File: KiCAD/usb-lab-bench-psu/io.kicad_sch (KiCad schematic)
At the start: 14 parts, among them J9 X077-6428TSWCG01-H13, Q6 2N7002K, Q7 BSS84

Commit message: updated GND and supply nets, switched buck-boost-converter
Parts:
- renumbered C41 to C30, C42 to C31, C43 to C32, C47 to C33, C48 to C34, Q6 to Q3, Q7 to Q4, R54 to R34, R53 to R35, R49 to R36, R50 to R37, R51 to R38, R52 to R39
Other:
- removed sheet 3.3V Buck Converter1
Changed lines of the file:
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@@
 		(dnp no)
 		(fields_autoplaced yes)
-		(property "Reference" "R53"
+		(property "Reference" "R35"
 			(at 35.56 34.2899 0)
 			(effects
@@
 			(project ""
 				(path "/63928bc9-e618-488a-a687-c6d5597f31d9/a5b1ba07-0ccc-4e60-84be-65366c488a00"
-					(reference "R53")
+					(reference "R35")
 					(unit 1)
 				)
@@
 		(on_board yes)
 		(dnp no)
-		(property "Reference" "R51"
+		(property "Reference" "R38"
 			(at 201.295 64.77 90)
 			(effects
@@
 			(project "usb-lab-bench-psu"
 				(path "/63928bc9-e618-488a-a687-c6d5597f31d9/a5b1ba07-0ccc-4e60-84be-65366c488a00"
-					(reference "R51")
+					(reference "R38")
 					(unit 1)
 				)
@@
 		(dnp no)
 		(fields_autoplaced yes)
-		(property "Reference" "R50"
+		(property "Reference" "R37"
 			(at 101.6 33.02 90)
 			(effects
@@
 			(project "usb-lab-bench-psu"
 				(path "/63928bc9-e618-488a-a687-c6d5597f31d9/a5b1ba07-0ccc-4e60-84be-65366c488a00"
-					(reference "R50")
+					(reference "R37")
 					(unit 1)
 				)
@@
 		(dnp no)
 		(fields_autoplaced yes)
-		(property "Reference" "C48"
+		(property "Reference" "C34"
 			(at 166.37 78.7399 0)
 			(effects
@@
 			(project "usb-lab-bench-psu"
 				(path "/63928bc9-e618-488a-a687-c6d5597f31d9/a5b1ba07-0ccc-4e60-84be-65366c488a00"
-					(reference "C48")
+					(reference "C34")
 					(unit 1)
 				)
@@
 		(dnp no)
 		(fields_autoplaced yes)
-		(property "Reference" "Q6"
+		(property "Reference" "Q3"
 			(at 114.3 46.9899 0)
 			(effects
@@
 			(project "usb-lab-bench-psu"
 				(path "/63928bc9-e618-488a-a687-c6d5597f31d9/a5b1ba07-0ccc-4e60-84be-65366c488a00"
-					(reference "Q6")
+					(reference "Q3")
 					(unit 1)
 				)
@@
 		(dnp no)
 		(fields_autoplaced yes)
-		(property "Reference" "C41"
+		(property "Reference" "C30"
 			(at 133.35 58.4199 0)
 			(effects
@@
 			(project "usb-lab-bench-psu"
 				(path "/63928bc9-e618-488a-a687-c6d5597f31d9/a5b1ba07-0ccc-4e60-84be-65366c488a00"
-					(reference "C41")
+					(reference "C30")
 					(unit 1)
 				)
@@
 		(dnp no)
 		(fields_autoplaced yes)
-		(property "Reference" "Q7"
+		(property "Reference" "Q4"
 			(at 133.35 38.0999 0)
 			(effects
@@
 			(project "usb-lab-bench-psu"
 				(path "/63928bc9-e618-488a-a687-c6d5597f31d9/a5b1ba07-0ccc-4e60-84be-65366c488a00"
-					(reference "Q7")
+					(reference "Q4")
 					(unit 1)
 				)
@@
 		(dnp no)
 		(fields_autoplaced yes)
-		(property "Reference" "C47"
+		(property "Reference" "C33"
 			(at 156.21 58.4199 0)
 			(effects
@@
 			(project "usb-lab-bench-psu"
 				(path "/63928bc9-e618-488a-a687-c6d5597f31d9/a5b1ba07-0ccc-4e60-84be-65366c488a00"
-					(reference "C47")
+					(reference "C33")
 					(unit 1)
 				)
@@
 		(on_board yes)
 		(dnp no)
-		(property "Reference" "R52"
+		(property "Reference" "R39"
 			(at 210.185 64.77 90)
 			(effects
@@
 			(project "usb-lab-bench-psu"
 				(path "/63928bc9-e618-488a-a687-c6d5597f31d9/a5b1ba07-0ccc-4e60-84be-65366c488a00"
-					(reference "R52")
+					(reference "R39")
 					(unit 1)
 				)
@@
 		(on_board yes)
 		(dnp no)
-		(property "Reference" "R54"
+		(property "Reference" "R34"
 			(at 24.384 34.29 0)
 			(effects
@@
 			(project "usb-lab-bench-psu"
 				(path "/63928bc9-e618-488a-a687-c6d5597f31d9/a5b1ba07-0ccc-4e60-84be-65366c488a00"
-					(reference "R54")
+					(reference "R34")
 					(unit 1)
 				)
@@
 		(on_board yes)
 		(dnp no)
-		(property "Reference" "C43"
+		(property "Reference" "C32"
 			(at 154.94 78.74 0)
 			(effects
@@
 			(project "usb-lab-bench-psu"
 				(path "/63928bc9-e618-488a-a687-c6d5597f31d9/a5b1ba07-0ccc-4e60-84be-65366c488a00"
-					(reference "C43")
+					(reference "C32")
 					(unit 1)
 				)
@@
 		(dnp no)
 		(fields_autoplaced yes)
-		(property "Reference" "R49"
+		(property "Reference" "R36"
 			(at 96.52 53.3399 0)
 			(effects
@@
 			(project "usb-lab-bench-psu"
 				(path "/63928bc9-e618-488a-a687-c6d5597f31d9/a5b1ba07-0ccc-4e60-84be-65366c488a00"
-					(reference "R49")
+					(reference "R36")
 					(unit 1)
 				)
@@
 		(dnp no)
 		(fields_autoplaced yes)
-		(property "Reference" "C42"
+		(property "Reference" "C31"
 			(at 144.78 58.4199 0)
 			(effects
@@
 			(project "usb-lab-bench-psu"
 				(path "/63928bc9-e618-488a-a687-c6d5597f31d9/a5b1ba07-0ccc-4e60-84be-65366c488a00"
-					(reference "C42")
-					(unit 1)
-				)
-			)
-		)
-	)
-	(sheet
-		(at 34.29 24.13)
-		(size 35.56 25.4)
-		(fields_autoplaced yes)
-		(stroke
-			(width 0.1524)
-			(type solid)
-		)
-		(fill
-			(color 0 0 0 0.0000)
-		)
-		(property "Sheetname" "3.3V Buck Converter1"
-			(at 34.29 23.4184 0)
-			(effects
-				(font
-					(size 1.27 1.27)
-				)
-				(justify left bottom)
-			)
-		)
-		(property "Sheetfile" "buck_converter.kicad_sch"
-			(at 34.29 50.1146 0)
-			(effects
-				(font
-					(size 1.27 1.27)
-				)
-				(justify left top)
-			)
-		)
-		(pin "V-OUT" input
-			(at 69.85 29.21 0)
-			(effects
-				(font
-					(size 1.27 1.27)
-				)
-				(justify right)
-			)
-		)
-		(pin "VIN_2" output
-			(at 34.29 31.75 180)
-			(effects
-				(font
-					(size 1.27 1.27)
-				)
-				(justify left)
-			)
-		)
-		(pin "VIN_2_ACTIVE" input
-			(at 69.85 44.45 0)
-			(effects
-				(font
-					(size 1.27 1.27)
-				)
-				(justify right)
-			)
-		)
-		(pin "VIN_2_IMON" input
-			(at 69.85 46.99 0)
-			(effects
-				(font
-					(size 1.27 1.27)
-				)
-				(justify right)
-			)
-		)
-		(pin "VIN_1" output
-			(at 34.29 29.21 180)
-			(effects
-				(font
-					(size 1.27 1.27)
-				)
-				(justify left)
-			)
-		)
-		(pin "VIN_1_IMON" input
-			(at 69.85 39.37 0)
-			(effects
-				(font
-					(size 1.27 1.27)
-				)
-				(justify right)
-			)
-		)
-		(pin "VIN_1_ACTIVE" input
-			(at 69.85 36.83 0)
-			(effects
-				(font
-					(size 1.27 1.27)
-				)
-				(justify right)
-			)
-		)
-		(pin "GND" passive
-			(at 34.29 40.64 180)
-			(effects
-				(font
-					(size 1.27 1.27)
-				)
-				(justify left)
-			)
-		)
-		(instances
-			(project "usb-lab-bench-psu"
-				(path "/63928bc9-e618-488a-a687-c6d5597f31d9/a5b1ba07-0ccc-4e60-84be-65366c488a00"
-					(page "8")
-				)
-			)
+					(reference "C31")
+					(unit 1)
+				)
+			)

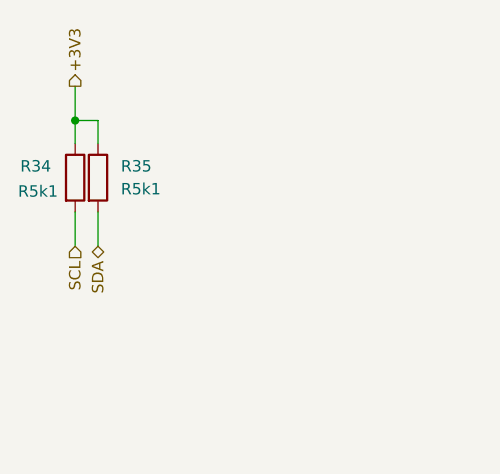
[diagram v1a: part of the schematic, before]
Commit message: added current limitting feedback circuit
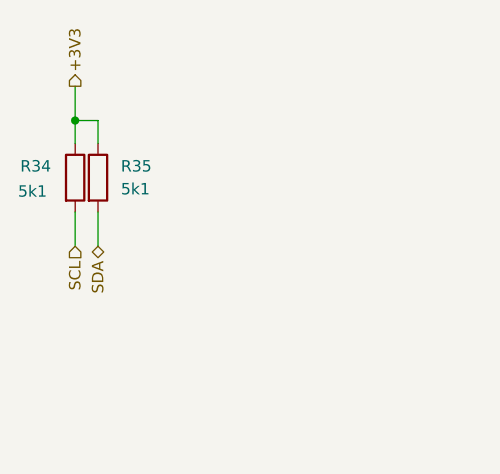
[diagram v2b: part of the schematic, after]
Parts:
- R34, R35: value R5k1 -> 5k1
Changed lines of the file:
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@@
 			)
 		)
-		(property "Value" "R5k1"
+		(property "Value" "5k1"
 			(at 35.56 36.8299 0)
 			(effects
@@
 			)
 		)
-		(property "Value" "R5k1"
+		(property "Value" "5k1"
 			(at 24.13 37.084 0)
 			(effects

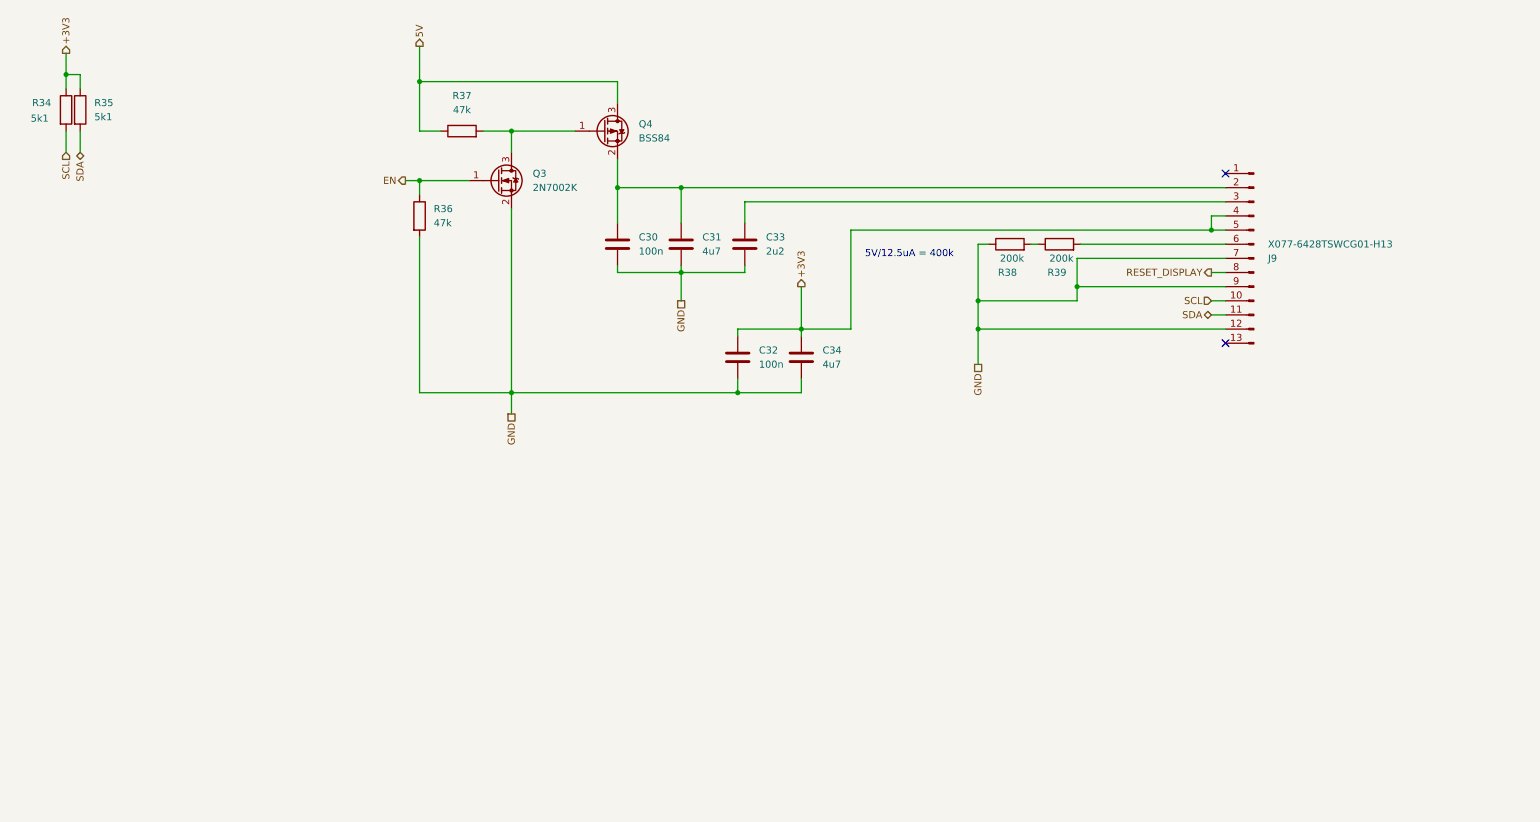
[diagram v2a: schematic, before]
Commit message: adapted buck converter
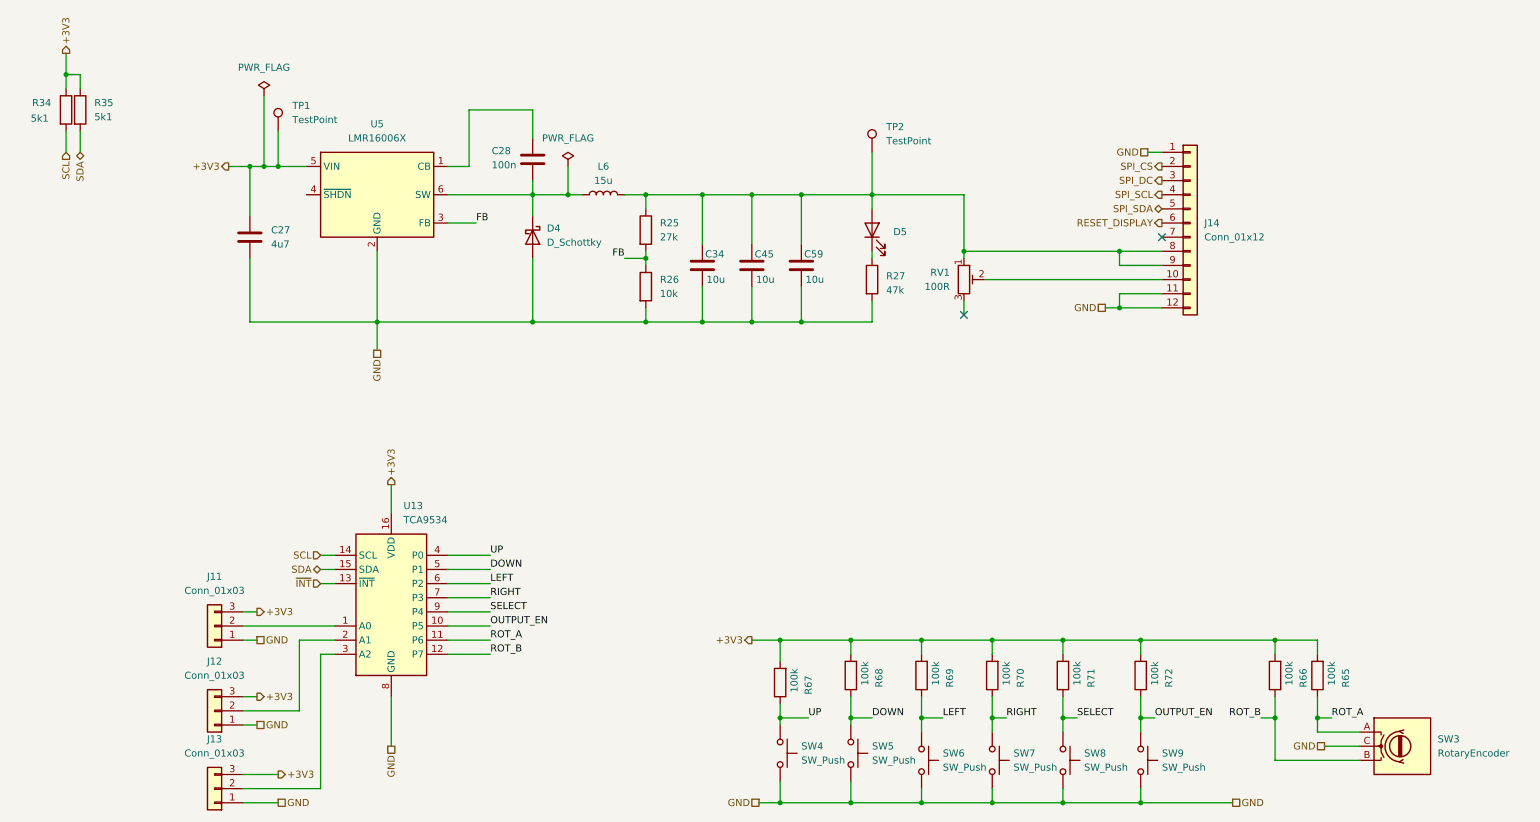
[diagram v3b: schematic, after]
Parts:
- removed C30, C32: 100n, Capacitor_SMD:C_0402_1005Metric_Pad0.74x0.62mm_HandSolder, symbol Device:C
- removed C31: 4u7, Capacitor_SMD:C_0402_1005Metric_Pad0.74x0.62mm_HandSolder, symbol Device:C
- removed C33: 2u2, Capacitor_SMD:C_0402_1005Metric_Pad0.74x0.62mm_HandSolder, symbol Device:C
- removed J9: X077-6428TSWCG01-H13, Prj_display:X077-6428TSWCG01-H13, symbol Connector:Conn_01x13_Male
- removed Q3: 2N7002K, Package_TO_SOT_SMD:SOT-23, symbol Transistor_FET:2N7002K
- removed Q4: BSS84, Package_TO_SOT_SMD:SOT-23, symbol Transistor_FET:BSS84
- removed R36, R37: 47k, Resistor_SMD:R_0402_1005Metric_Pad0.72x0.64mm_HandSolder, symbol Device:R
- removed R38, R39: 200k, Resistor_SMD:R_0402_1005Metric_Pad0.72x0.64mm_HandSolder, symbol Device:R
- added C27: 4u7, symbol Device:C
- added C28: 100n, symbol Device:C
- added C45, C59: 10u, symbol Device:C
- added D4: D_Schottky, symbol Device:D_Schottky
- added D5: XL-1005UGC, Diode_SMD:D_0402_1005Metric_Pad0.77x0.64mm_HandSolder, symbol Device:LED
- added J11, J12, J13: Conn_01x03, symbol Connector_Generic:Conn_01x03
- added J14: Conn_01x12, symbol Connector_Generic:Conn_01x12
- added L6: 15u, symbol Device:L
- added R25: 27k, Resistor_SMD:R_0402_1005Metric_Pad0.72x0.64mm_HandSolder, symbol Device:R
- added R26: 10k, Resistor_SMD:R_0402_1005Metric_Pad0.72x0.64mm_HandSolder, symbol Device:R
- added R27: 47k, Resistor_SMD:R_0402_1005Metric_Pad0.72x0.64mm_HandSolder, symbol Device:R
- added R65, R66, R67, R68, R69, R70, R71, R72: 100k, Resistor_SMD:R_0402_1005Metric_Pad0.72x0.64mm_HandSolder, symbol Device:R
- added RV1: 100R, symbol Device:R_Potentiometer_Trim
- added SW3: RotaryEncoder, symbol Device:RotaryEncoder
- added SW4, SW5, SW6, SW7, SW8, SW9: SW_Push, symbol Switch:SW_Push
- added TP1, TP2: TestPoint, symbol Connector:TestPoint
- added U13: TCA9534, symbol Interface_Expansion:TCA9534
- added U5: LMR16006X, Package_TO_SOT_SMD:TSOT-23-6, symbol Prj_dcdc_converter:LMR16006X
- C34: value 4u7 -> 10u; footprint Capacitor_SMD:C_0402_1005Metric_Pad0.74x0.62mm_HandSolder -> (none)
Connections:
- net +3V3: now also C27.1, J11.3 (Pin_3), J12.3 (Pin_3), J13.3 (Pin_3), R65.2, R66.2, R67.2, R68.2, R69.2, R70.2, R71.2, R72.2, TP1.1, U13.16 (VDD), U5.5 (VIN); no longer C34.1
- net GND: now also C27.2, C45.2, C59.2, D4.2 (A), J11.1 (Pin_1), J12.1 (Pin_1), J13.1 (Pin_1), J14.1 (Pin_1), J14.11 (Pin_11), J14.12 (Pin_12), R26.2, R27.2, SW3.C, SW4.2, SW5.2, SW6.2, SW7.2, SW8.2, SW9.2, U13.8 (GND), U5.2 (GND)
- net RESET_DISPLAY: now also J14.6 (Pin_6)
- net SCL: now also U13.14 (SCL)
- net SDA: now also U13.15 (SDA)
- new net: C28.2, D4.1 (K), L6.1, U5.6 (SW)
- new net: J12.2 (Pin_2), U13.2 (A1)
- new net: C34.1, C45.1, C59.1, D5.2 (A), J14.8 (Pin_8), J14.9 (Pin_9), L6.2, R25.1, RV1.1, TP2.1
- new net: J11.2 (Pin_2), U13.1 (A0)
- new net: J13.2 (Pin_2), U13.3 (A2)
- new net: C28.1, U5.1 (CB)
- new net: J14.10 (Pin_10), RV1.2
- new net: D5.1 (K), R27.1
- new net DOWN: R68.1, SW5.1, U13.5 (P1)
- new net FB: R25.2, R26.1, U5.3 (FB)
- new net LEFT: R69.1, SW6.1, U13.6 (P2)
- new net OUTPUT_EN: R72.1, SW9.1, U13.10 (P5)
- new net RIGHT: R70.1, SW7.1, U13.7 (P3)
- new net ROT_A: R65.1, SW3.A, U13.11 (P6)
- new net ROT_B: R66.1, SW3.B, U13.12 (P7)
- new net SELECT: R71.1, SW8.1, U13.9 (P4)
- new net SPI_CS: J14.2 (Pin_2)
- new net SPI_DC: J14.3 (Pin_3)
- new net SPI_SCL: J14.4 (Pin_4)
- new net SPI_SDA: J14.5 (Pin_5)
- new net UP: R67.1, SW4.1, U13.4 (P0)
- new net ~{INT}: U13.13 (~{INT})
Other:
- note removed: "5V/12.5uA = 400k"

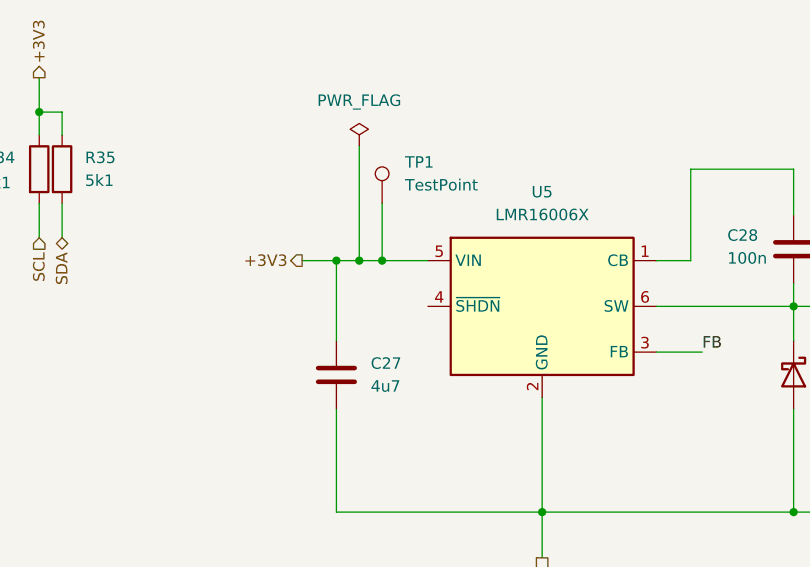
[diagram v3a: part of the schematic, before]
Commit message: restructured schematics to better show individual boards
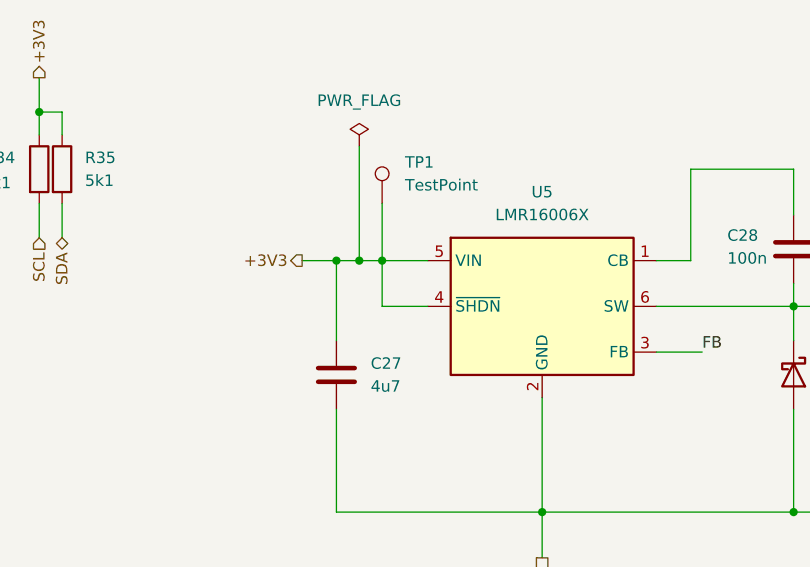
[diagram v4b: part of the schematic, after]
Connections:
- net +3V3: now also U5.4 (~{SHDN})
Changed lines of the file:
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@@
+	(wire
+		(pts
+			(xy 73.66 50.8) (xy 68.58 50.8)
+		)
+		(stroke
+			(width 0)
+			(type default)
+		)
+	)
 	(wire
 		(pts
@@
 		)
 		(stroke
+			(width 0)
+			(type default)
+		)
+	)
+	(wire
+		(pts
+			(xy 68.58 50.8) (xy 68.58 45.72)
+		)
+		(stroke
